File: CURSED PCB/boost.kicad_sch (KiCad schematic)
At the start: 6 parts, among them U11 TPS61046YFFR

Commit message: updated schematic
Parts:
- added U9: TPS61046YFFR, YFF0006AAAA, symbol TPS61046YFFR:TPS61046YFFR
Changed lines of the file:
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@@
+	)
+	(symbol
+		(lib_id "TPS61046YFFR:TPS61046YFFR")
+		(at 57.15 134.62 0)
+		(unit 1)
+		(exclude_from_sim no)
+		(in_bom yes)
+		(on_board yes)
+		(dnp no)
+		(fields_autoplaced yes)
+		(property "Reference" "U9"
+			(at 57.15 114.3 0)
+			(effects
+				(font
+					(size 1.524 1.524)
+				)
+			)
+		)
+		(property "Value" "TPS61046YFFR"
+			(at 57.15 116.84 0)
+			(effects
+				(font
+					(size 1.524 1.524)
+				)
+			)
+		)
+		(property "Footprint" "YFF0006AAAA"
+			(at 57.15 134.62 0)
+			(effects
+				(font
+					(size 1.27 1.27)
+					(italic yes)
+				)
+				(hide yes)
+			)
+		)
+		(property "Datasheet" "https://www.ti.com/lit/gpn/tps61046"
+			(at 57.15 134.62 0)
+			(effects
+				(font
+					(size 1.27 1.27)
+					(italic yes)
+				)
+				(hide yes)
+			)
+		)
+		(property "Description" ""
+			(at 57.15 134.62 0)
+			(effects
+				(font
+					(size 1.27 1.27)
+				)
+				(hide yes)
+			)
+		)
+		(pin "A1"
+		)
+		(pin "B2"
+		)
+		(pin "C1"
+		)
+		(pin "C2"
+		)
+		(pin "B1"
+		)
+		(pin "A2"
+		)
+		(instances
+			(project ""
+				(path "/9fb1a86f-679c-4b88-9ed1-932f4f414580/a884d289-6403-4974-bfe5-5c532984589b"
+					(reference "U9")
+					(unit 1)
+				)
+			)
+		)
 	)
 	(symbol

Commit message: UPDATE
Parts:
- removed U9: TPS61046YFFR, YFF0006AAAA, symbol TPS61046YFFR:TPS61046YFFR
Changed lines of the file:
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@@
-	)
-	(symbol
-		(lib_id "TPS61046YFFR:TPS61046YFFR")
-		(at 57.15 134.62 0)
-		(unit 1)
-		(exclude_from_sim no)
-		(in_bom yes)
-		(on_board yes)
-		(dnp no)
-		(fields_autoplaced yes)
-		(property "Reference" "U9"
-			(at 57.15 114.3 0)
-			(effects
-				(font
-					(size 1.524 1.524)
-				)
-			)
-		)
-		(property "Value" "TPS61046YFFR"
-			(at 57.15 116.84 0)
-			(effects
-				(font
-					(size 1.524 1.524)
-				)
-			)
-		)
-		(property "Footprint" "YFF0006AAAA"
-			(at 57.15 134.62 0)
-			(effects
-				(font
-					(size 1.27 1.27)
-					(italic yes)
-				)
-				(hide yes)
-			)
-		)
-		(property "Datasheet" "https://www.ti.com/lit/gpn/tps61046"
-			(at 57.15 134.62 0)
-			(effects
-				(font
-					(size 1.27 1.27)
-					(italic yes)
-				)
-				(hide yes)
-			)
-		)
-		(property "Description" ""
-			(at 57.15 134.62 0)
-			(effects
-				(font
-					(size 1.27 1.27)
-				)
-				(hide yes)
-			)
-		)
-		(pin "A1"
-		)
-		(pin "B2"
-		)
-		(pin "C1"
-		)
-		(pin "C2"
-		)
-		(pin "B1"
-		)
-		(pin "A2"
-		)
-		(instances
-			(project ""
-				(path "/9fb1a86f-679c-4b88-9ed1-932f4f414580/a884d289-6403-4974-bfe5-5c532984589b"
-					(reference "U9")
-					(unit 1)
-				)
-			)
-		)
 	)
 	(symbol

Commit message: updated schematic
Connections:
- net V_AMP_OUT renamed +24V
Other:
- note removed: "24V"
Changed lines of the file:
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@@
 	(generator_version "9.0")
 	(paper "A4")
-	(text "24V"
+	(text "Name: TPS61046YFFR\nidk why its not updating"
 		(exclude_from_sim no)
-		(at 152.908 100.584 0)
+		(at 124.46 95.25 0)
 		(effects
 			(font
@@
 		)
 	)
-	(text "Name: TPS61046YFFR\nidk why its not updating"
-		(exclude_from_sim no)
-		(at 120.396 95.25 0)
-		(effects
-			(font
-				(size 1.27 1.27)
-			)
-		)
-	)
 	(junction
 		(at 81.28 101.6)
@@
 	)
 	(junction
+		(at 95.25 127)
+		(diameter 0)
+		(color 0 0 0 0)
+	)
+	(junction
 		(at 134.62 104.14)
 		(diameter 0)
@@
 	)
 	(junction
-		(at 95.25 127)
-		(diameter 0)
-		(color 0 0 0 0)
-	)
-	(junction
 		(at 120.65 127)
 		(diameter 0)
@@
 	(wire
 		(pts
+			(xy 154.94 104.14) (xy 154.94 92.71)
+		)
+		(stroke
+			(width 0)
+			(type default)
+		)
+	)
+	(wire
+		(pts
 			(xy 81.28 101.6) (xy 87.63 101.6)
 		)
@@
 	(wire
 		(pts
-			(xy 134.62 104.14) (xy 152.4 104.14)
+			(xy 134.62 104.14) (xy 154.94 104.14)
 		)
 		(stroke
@@
 	(wire
 		(pts
-			(xy 134.62 111.76) (xy 134.62 104.14)
+			(xy 134.62 104.14) (xy 134.62 111.76)
 		)
 		(stroke
@@
 			(width 0)
 			(type default)
-		)
-	)
-	(hierarchical_label "V_AMP_OUT"
-		(shape output)
-		(at 152.4 104.14 0)
-		(effects
-			(font
-				(size 1.27 1.27)
-			)
-			(justify left)
 		)
 	)
@@
 					(unit 1)
 				)
+			)
+		)
+	)
+	(symbol
+		(lib_id "power:+24V")
+		(at 154.94 92.71 0)
+		(unit 1)
+		(exclude_from_sim no)
+		(in_bom yes)
+		(on_board yes)
+		(dnp no)
+		(fields_autoplaced yes)
+		(property "Reference" "#PWR053"
+			(at 154.94 96.52 0)
+			(effects
+				(font
+					(size 1.27 1.27)
+				)
+				(hide yes)
+			)
+		)
+		(property "Value" "+24V"
+			(at 154.94 87.63 0)
+			(effects
+				(font
+					(size 1.27 1.27)
+				)
+			)
+		)
+		(property "Footprint" ""
+			(at 154.94 92.71 0)
+			(effects
+				(font
+					(size 1.27 1.27)
+				)
+				(hide yes)
+			)
+		)
+		(property "Datasheet" ""
+			(at 154.94 92.71 0)
+			(effects
+				(font
+					(size 1.27 1.27)
+				)
+				(hide yes)
+			)
+		)
+		(property "Description" "Power symbol creates a global label with name \"+24V\""
+			(at 154.94 92.71 0)
+			(effects
+				(font
+					(size 1.27 1.27)
+				)
+				(hide yes)
+			)
+		)
+		(pin "1"
+		)
+		(instances
+			(project "sensor_1"
+				(path "/9fb1a86f-679c-4b88-9ed1-932f4f414580/a884d289-6403-4974-bfe5-5c532984589b"
+					(reference "#PWR053")
+					(unit 1)
+				)

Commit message: schematic changes
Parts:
- L1: footprint MLF1608E120JTD25:IND_1608_TDK -> LBM2016T120J:INDC2016X180N
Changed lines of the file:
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@@
 			)
 		)
-		(property "Footprint" "MLF1608E120JTD25:IND_1608_TDK"
+		(property "Footprint" "LBM2016T120J:INDC2016X180N"
 			(at 95.25 88.9 0)
 			(effects

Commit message: footprint folde rupdate
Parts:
- C19: footprint Capacitor_SMD:C_0805_2012Metric_Pad1.18x1.45mm_HandSolder -> EMK107B7105KA-T:CAPC1608X90N
- C20: footprint Capacitor_SMD:C_0805_2012Metric_Pad1.18x1.45mm_HandSolder -> MCASU31LSB5105KTNA01:CAPC3216X180N
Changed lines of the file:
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@@
 			)
 		)
-		(property "Footprint" "Capacitor_SMD:C_0805_2012Metric_Pad1.18x1.45mm_HandSolder"
+		(property "Footprint" "EMK107B7105KA-T:CAPC1608X90N"
 			(at 64.4652 111.76 0)
 			(effects
@@
 			)
 		)
-		(property "Footprint" "Capacitor_SMD:C_0805_2012Metric_Pad1.18x1.45mm_HandSolder"
+		(property "Footprint" "MCASU31LSB5105KTNA01:CAPC3216X180N"
 			(at 135.5852 119.38 0)
 			(effects

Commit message: updates traces and footprints
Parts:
- L1: footprint LBM2016T120J:INDC2016X180N -> ul_NRH3010T100MN:IND_TAIYO_NRH3010_TAY
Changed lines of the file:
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@@
 			)
 		)
-		(property "Footprint" "LBM2016T120J:INDC2016X180N"
+		(property "Footprint" "ul_NRH3010T100MN:IND_TAIYO_NRH3010_TAY"
 			(at 95.25 88.9 0)
 			(effects

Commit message: updated booster
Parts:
- removed U11: TPS61046YFFR, Package_SON:WSON-6-1EP_2x2mm_P0.65mm_EP1x1.6mm, symbol Regulator_Switching:TPS610995DRV
- added U9: TLV61046ADBVR, TLV61046A:SOT95P280X145-6N, symbol TLV61046A:TLV61046ADBVR
- L1: value 12uH -> 10uH
- R12: value 120k -> 71.5K
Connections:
- net +24V: now also U9.5 (VOUT)
- net +5V: now also U9.4 (EN), U9.6 (VIN)
- net GND: now also U9.2 (GND)
- net at L1.2: now also U9.1 (SW)
- net at R12.2, R13.1: now also U9.3 (FB)
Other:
- note added: "Reference photos, calculations all in Payload Experimental & PCB Data Setup Master under Booster sheet"
- note removed: "Name: TPS61046YFFR idk why its not updating"
- moved on the sheet: C19, C20, L1, R12, R13

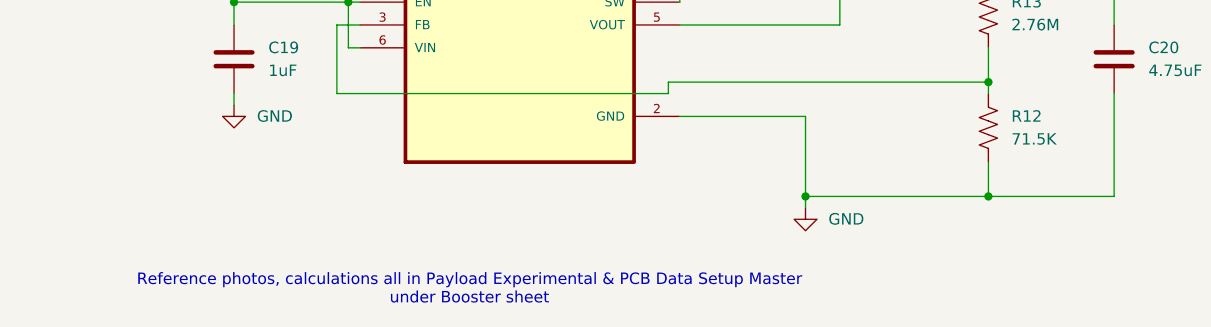
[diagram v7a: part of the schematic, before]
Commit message: Updated PDF and make schematic look more pretty
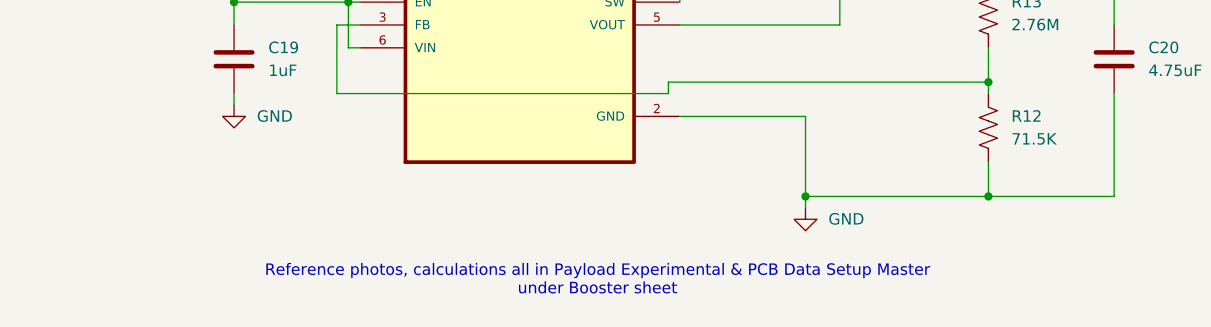
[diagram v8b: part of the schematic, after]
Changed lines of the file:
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@@
 	(text "Reference photos, calculations all in Payload Experimental & PCB Data Setup Master\nunder Booster sheet"
 		(exclude_from_sim no)
-		(at 61.722 153.924 0)
+		(at 75.946 152.908 0)
 		(effects
 			(font
